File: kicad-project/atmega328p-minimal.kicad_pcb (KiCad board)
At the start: 2 copper layers, 22.9 x 48.3 mm, 9 parts, among them IC1 ATMEGA328-P, P1 CONN_01X02, P2 CONN_01X16, P3 CONN_01X16, SW1 SW_PUSH, Y1 16MHz

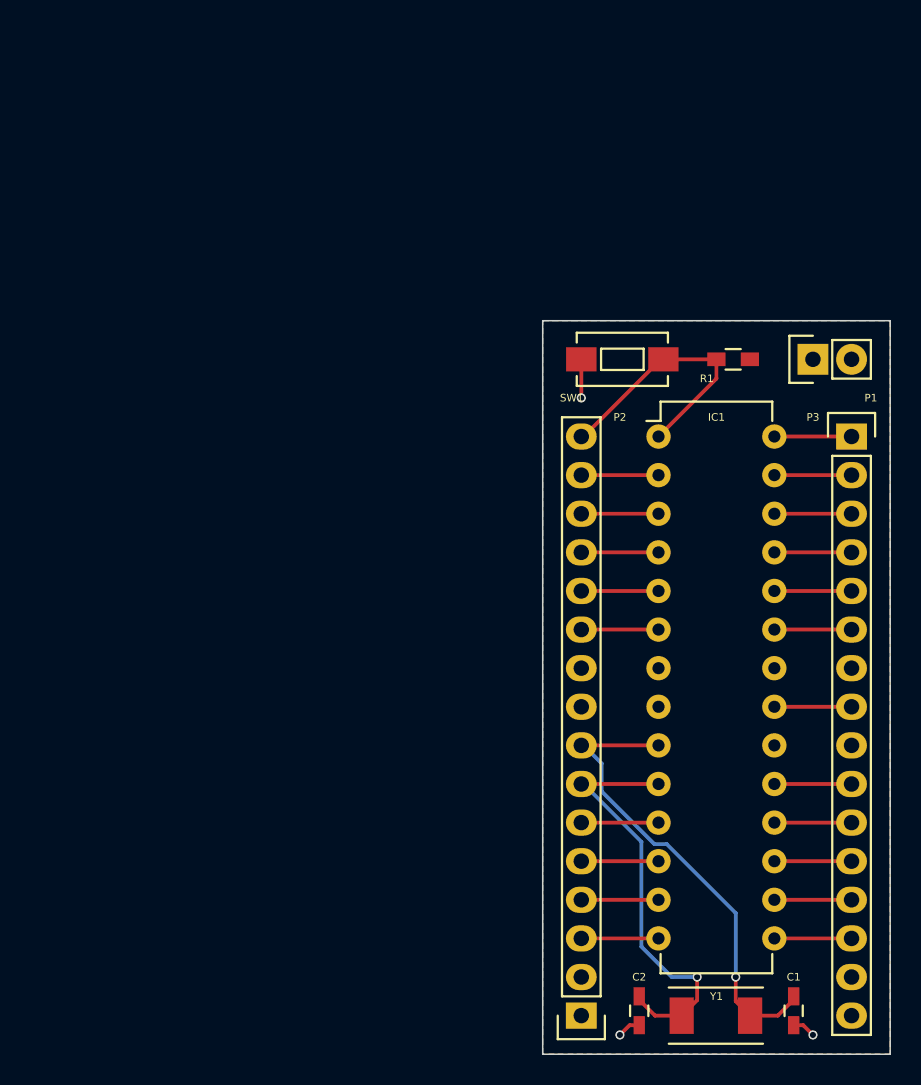
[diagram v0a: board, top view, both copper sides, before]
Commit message: Fixed missing sheet information and revision.
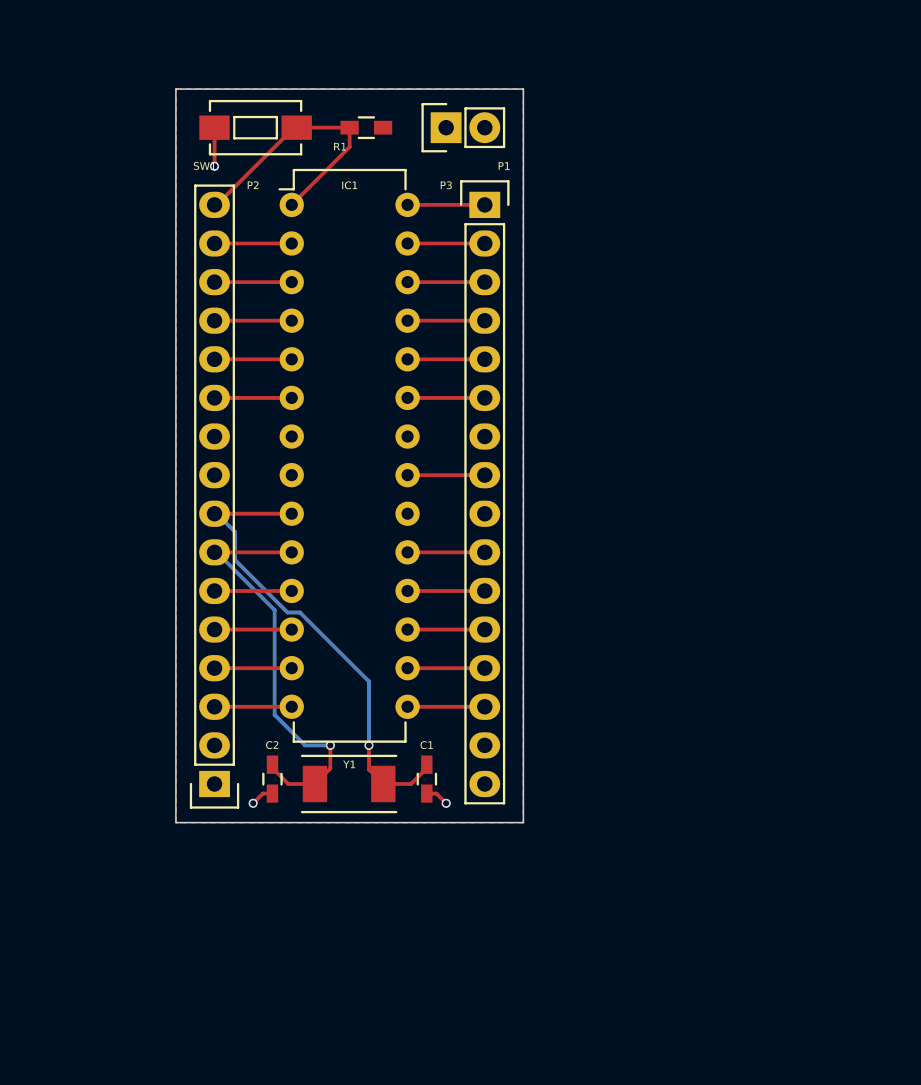
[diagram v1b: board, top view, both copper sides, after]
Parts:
- moved C1 28.5 mm to (157.5, 124.1)
- moved C2 28.5 mm to (147.3, 124.1)
- moved IC1 28.5 mm to (148.6, 86.4)
- moved P1 28.5 mm to (158.8, 81.3)
- moved P2 28.5 mm to (143.5, 124.5)
- moved P3 28.5 mm to (161.3, 86.4)
- moved R1 28.5 mm to (153.5, 81.3)
- moved SW1 28.5 mm to (146.2, 81.3)
- moved Y1 28.5 mm to (152.4, 124.5)

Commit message: Changed KiCad project, schematics and board design for this version.
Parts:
- removed IC1: ATMEGA328-P, Housings_DIP:DIP-28_W7.62mm
- removed P1: CONN_01X02, Pin_Headers:Pin_Header_Straight_1x02
- added U1: MCU-ATMEGA328P-PU_DIP28_, SeeedOPL-IC-2016:DIP28-2.54-34.7X7.62MM, F.Cu at (146.1, 100.3)
- C1, C2: footprint Capacitors_SMD:C_0603_HandSoldering -> Capacitors_SMD:C_0603
- R1: footprint Resistors_SMD:R_0603_HandSoldering -> Resistors_SMD:R_0603
- SW1: value SW_PUSH -> SMD-BUTTON_4P-5.2X5.2X1.5MM-SKQGADE010_; footprint Buttons_Switches_SMD:SW_SPST_EVQPE1 -> SeeedOPL-Switch-2016:SW4-SMD-5.2X5.2X1.5MM
- Y1: value 16MHz -> DIP-CRYSTAL-16MHZ-18PF-30PPM-40R_HC49US_; footprint Crystals:Crystal_SMD_0603_2Pads_obsolete -> SeeedOPL-Crystal Oscillator-2016:HC49US
- moved C1 14.2 mm to (143.4, 125.7), turned to 180 degrees
- moved R1 13.9 mm to (139.7, 83.1), turned to 270 degrees
- moved P2 9.25 mm to (134.6, 121.9)
- moved Y1 6.81 mm to (146.1, 121.9)
- moved P3 4.58 mm to (157.5, 83.8)
- moved SW1 2.55 mm to (146.1, 78.7)
- moved C2 2.11 mm to (148.7, 125.7), turned to 0 degrees
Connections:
- C1 pad 1: GND -> Net-(C1-Pad1)
- C1 pad 2: /XTAL1 -> GND
- C2 pad 1: GND -> Net-(C2-Pad1)
- C2 pad 2: /XTAL2 -> GND
- P2 pad 1: +5V -> GND
- P2 pad 10: +5V -> GND
- P2 pad 2: +5V -> GND
- P2 pad 7: /XTAL2 -> GND
- P2 pad 8: /XTAL1 -> GND
- P2 pad 9: +5V -> GND
- P3 pad 10: /D13 -> /D13_SCK
- P3 pad 11: /D12 -> /D12_MISO
- P3 pad 12: /D11 -> /D11_MOSI
- P3 pad 15: GND -> +5V
- P3 pad 16: GND -> +5V
- P3 pad 7: GND -> +5V
- P3 pad 9: GND -> +5V
- SW1 pad 1: /RESET -> (no net)
- SW1 pad 2: GND -> /RESET
- Y1 pad 1: /XTAL2 -> Net-(C1-Pad1)
- Y1 pad 2: /XTAL1 -> Net-(C2-Pad1)
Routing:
- net /XTAL1: track 31.6 -> 0.00 mm, vias 1 -> 0
- net /XTAL2: track 28.4 -> 0.00 mm, vias 1 -> 0
- net Net-(C2-Pad1): track 0.00 -> 24.4 mm
- net Net-(C1-Pad1): track 0.00 -> 19.8 mm
- net /D13_SCK: track 0.00 -> 7.62 mm
- net /D12_MISO: track 0.00 -> 7.62 mm
- net /D11_MOSI: track 0.00 -> 7.62 mm
- net /D13: track 5.08 -> 0.00 mm
- net /D12: track 5.08 -> 0.00 mm
- net /D11: track 5.08 -> 0.00 mm
- net /D9: track 5.08 -> 7.62 mm
- net /D8: track 5.08 -> 7.62 mm
- net /D7: track 5.08 -> 7.62 mm
- net /D6: track 5.08 -> 7.62 mm
- net /D5: track 5.08 -> 7.62 mm
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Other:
- board size 22.9 x 48.3 mm -> 29.2 x 52.7 mm
- board text added: "+5V"
- board text added: "A0"
- board text added: "A1"
- board text added: "A2"
- board text added: "A3"
- board text added: "A4"
- board text added: "A5"
- board text added: "AREF"
- board text added: "ATmega328P Minimal Rev 0.2.1"
- board text added: "D0_RX"
- board text added: "D10"
- board text added: "D11_MOSI"
- board text added: "D12_MISO"
- board text added: "D13_SCK"
- board text added: "D1_TX"
- board text added: "D2"
- board text added: "D3"
- board text added: "D4"
- board text added: "D5"
- board text added: "D6"
- board text added: "D7"
- board text added: "D8"
- board text added: "D9"
- board text added: "GND"
- board text added: "RESET"
- board text added: "marcbperez.github.com"

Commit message: Bumped version to 0.3.0.
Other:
- board text added: "ATmega328P Minimal Rev 0.3.0"
- board text removed: "ATmega328P Minimal Rev 0.2.1"
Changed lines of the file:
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@@
     (links 44)
     (no_connects 0)
-    (area 166.954999 90.119999 196.265001 142.925001)
+    (area 127.892198 74.879999 163.191802 128.605)
     (thickness 1.6)
     (drawings 38)
@@
   (title_block
     (title "ATmega328P Minimal")
-    (date 2017-09-22)
-    (rev 0.2.1)
+    (date 2017-09-30)
+    (rev 0.3.0)
     (company "marcbperez, Widerware")
   )
@@
     (effects (font (size 0.4 0.4) (thickness 0.05)) (justify left))
   )
-  (gr_text "ATmega328P Minimal\nRev 0.2.1" (at 159.385 76.835) (layer F.SilkS)
+  (gr_text "ATmega328P Minimal\nRev 0.3.0" (at 159.385 76.835) (layer F.SilkS)
     (effects (font (size 0.4 0.4) (thickness 0.05)) (justify right))
   )
